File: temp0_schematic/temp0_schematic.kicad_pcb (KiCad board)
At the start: 2 copper layers, 64 x 94 mm, 16 parts, among them U1 Pro_Trinket_5V, U2 ESP-01, U3 oled_I2C_ssd1306, U4 hdc1080, U5 3.3V_REG

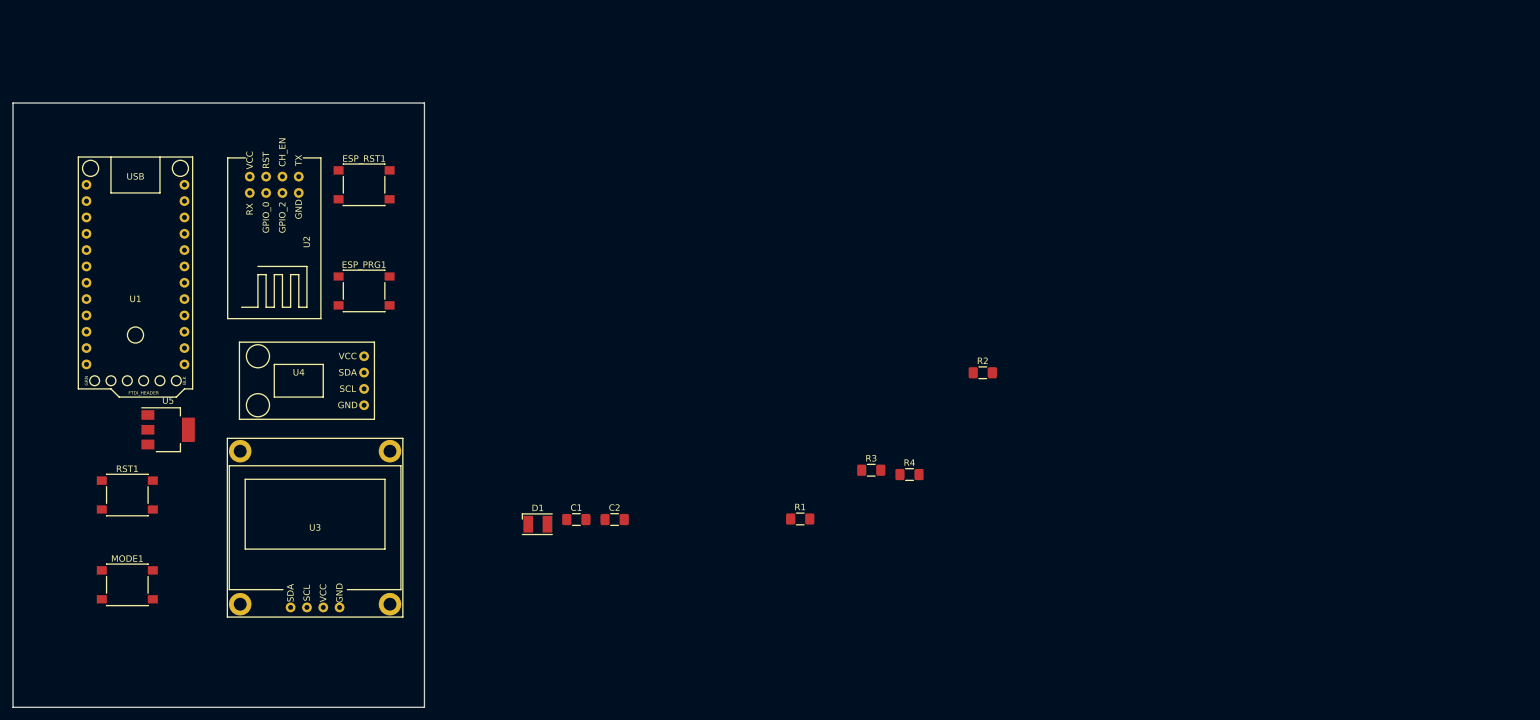
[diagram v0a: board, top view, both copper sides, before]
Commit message: Working on the schematic.  Added header for external button.
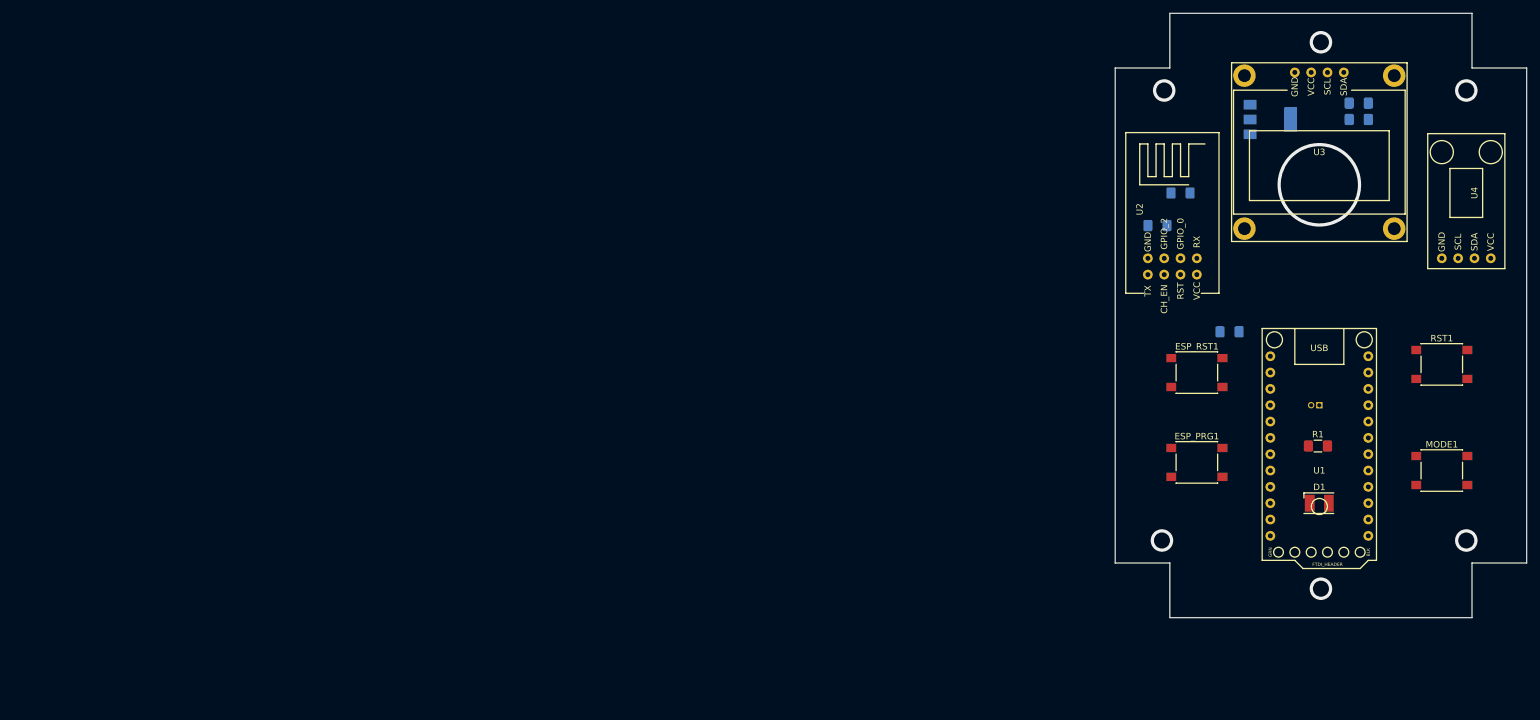
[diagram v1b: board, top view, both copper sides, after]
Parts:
- added J1: MODE1_EXT, Connector_PinHeader_1.27mm:PinHeader_1x02_P1.27mm_Horizontal, B.Cu at (233.7, 101.6)
- C1, C2, R2, R3, R4, U5: moved to B.Cu
- moved RST1 205.5 mm to (252.7, 95.2)
- moved MODE1 205.2 mm to (252.7, 111.8)
- moved U1 186.1 mm to (233.7, 108.0)
- moved U4 182.5 mm to (256.5, 69.8), turned to 90 degrees
- moved U5 178.1 mm to (226.1, 57.1)
- moved U3 166.8 mm to (233.7, 62.2), turned to 180 degrees
- moved U2 140.3 mm to (210.8, 80.0), turned to 270 degrees
- moved C1 137.9 mm to (239.8, 54.6)
- moved ESP_RST1 132.8 mm to (214.6, 96.5)
- moved ESP_PRG1 132.3 mm to (214.6, 110.5)
- moved C2 131.4 mm to (239.8, 57.1)
- moved D1 121.6 mm to (233.7, 116.8)
- moved R1 81.3 mm to (233.5, 108.0)
- moved R4 60.8 mm to (212.1, 68.6)
- moved R3 58.6 mm to (208.5, 73.7), turned to 180 degrees
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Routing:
- net (no net): vias 0 -> 7
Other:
- outline, holes or cut-outs redrawn

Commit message: Ran traces.
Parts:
- removed ESP_RST1: SW_Push, Button_Switch_SMD:SW_Push_1P1T_NO_6x6mm_H9.5mm
- added ESP_RST: SW_Push, Button_Switch_SMD:SW_Push_1P1T_NO_6x6mm_H9.5mm, F.Cu at (122.4, 105.4)
- J1: value MODE1_EXT -> MODE_EXT
- moved R2 96.8 mm to (123.2, 97.6), turned to 270 degrees
- moved U5 93.3 mm to (133.3, 67.3), turned to 270 degrees
- moved C2 93.0 mm to (147.5, 68.6)
- moved C1 92.8 mm to (147.5, 64.8)
- moved ESP_PRG 92.8 mm to (122.4, 120.7)
- moved U4 92.0 mm to (165.1, 80.0)
- moved R3 92.0 mm to (117.1, 83.8)
- moved U2 92.0 mm to (119.4, 90.2)
- moved U3 91.7 mm to (142.5, 72.0)
- moved D1 91.6 mm to (142.5, 125.7)
- moved U1 91.6 mm to (142.5, 116.8)
- moved R1 91.5 mm to (142.5, 118.1)
- moved J1 91.1 mm to (143.1, 111.8)
- moved RST 90.7 mm to (162.6, 105.4)
- moved MODE 90.6 mm to (162.6, 120.7)
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- renumbered ESP_PRG1 to ESP_PRG, MODE1 to MODE, RST1 to RST
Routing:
- net 3.3V: track 0.00 -> 100.4 mm, vias 0 -> 4
- net SCL: track 0.00 -> 94.1 mm
- net Net-(J1-Pad2): track 0.00 -> 90.0 mm
- net SDA: track 0.00 -> 87.8 mm
- net 5V: track 0.00 -> 70.4 mm
- net Net-(RST1-Pad2): track 0.00 -> 62.1 mm
- net Net-(ESP_PRG1-Pad2): track 0.00 -> 57.0 mm
- net U1_RX: track 0.00 -> 56.1 mm
- net U1_TX: track 0.00 -> 51.4 mm, vias 0 -> 1
- net Net-(ESP_RST1-Pad1): track 0.00 -> 22.3 mm, vias 0 -> 2
- net Net-(D1-Pad2): track 0.00 -> 15.3 mm, vias 0 -> 1
- net Net-(R3-Pad1): track 0.00 -> 8.98 mm
- net Net-(D1-Pad1): track 0.00 -> 7.63 mm
- added copper zone on B.Cu, net GND
- added copper zone on F.Cu, net GND
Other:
- net class Power added: clearance 0.2, trace_width 0.5, via_dia 1.6, via_drill 0.8

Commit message: Completed first attempt at pcb. Generated gerbers to order fab.
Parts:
- added G***: LOGO, temp0_parts:clewsy_logo_10mm, F.Cu at (149.9, 92.1)
- added U6: FTDI, Connector_PinHeader_2.54mm:PinHeader_1x06_P2.54mm_Horizontal, B.Cu at (128.3, 114.3)
- J1: footprint Connector_PinHeader_1.27mm:PinHeader_1x02_P1.27mm_Horizontal -> Connector_PinHeader_2.54mm:PinHeader_1x02_P2.54mm_Horizontal
- U3: value oled_I2C_ssd1306 -> SSD1306_128x64_OLED
- U4: value hdc1080 -> HDC1080
- moved J1 20.9 mm to (163.8, 114.3)
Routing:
- net 3.3V: track 100.4 -> 121.9 mm
- net U1_TX: track 51.4 -> 67.9 mm
- net Net-(J1-Pad2): track 90.0 -> 99.0 mm
- net U1_RX: track 56.1 -> 54.6 mm
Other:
- board text added: "clewsy 2020 clews.pro"

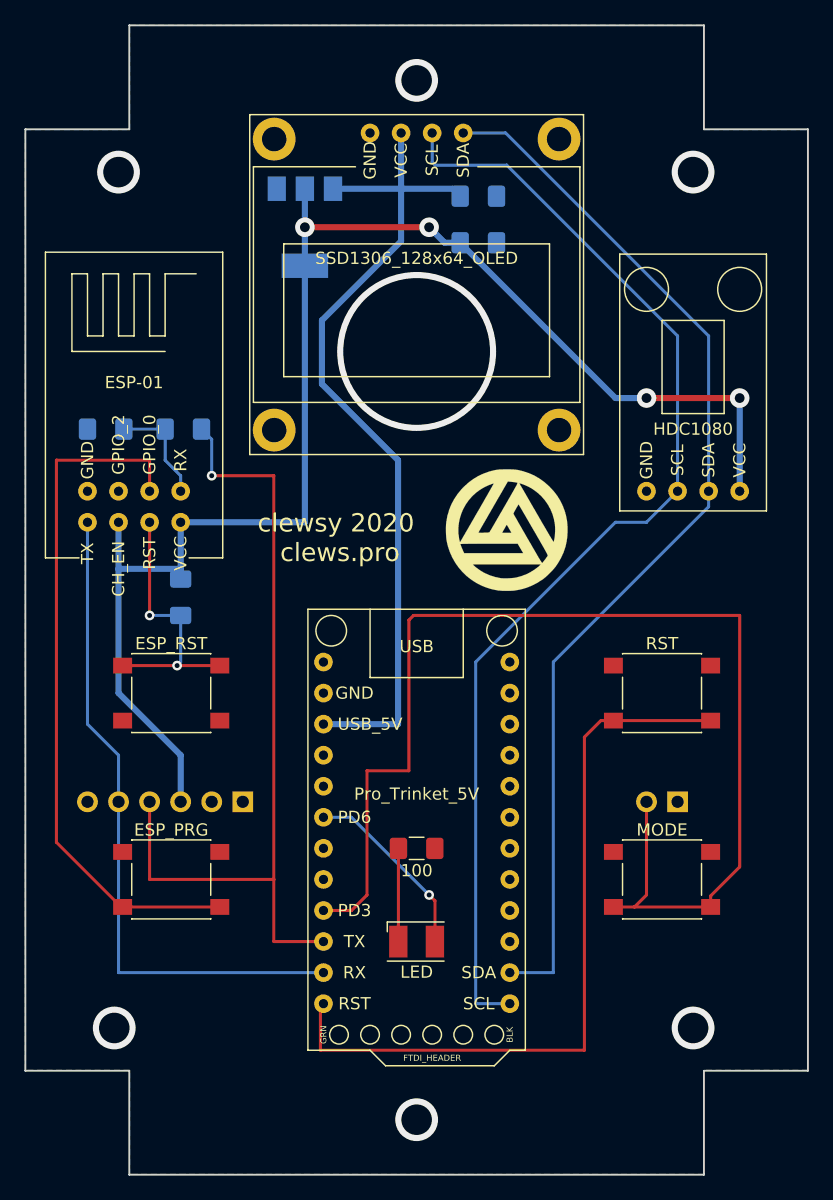
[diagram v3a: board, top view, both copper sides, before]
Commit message: PCB fixed - mount hole alignment, ftdi clearance, other.
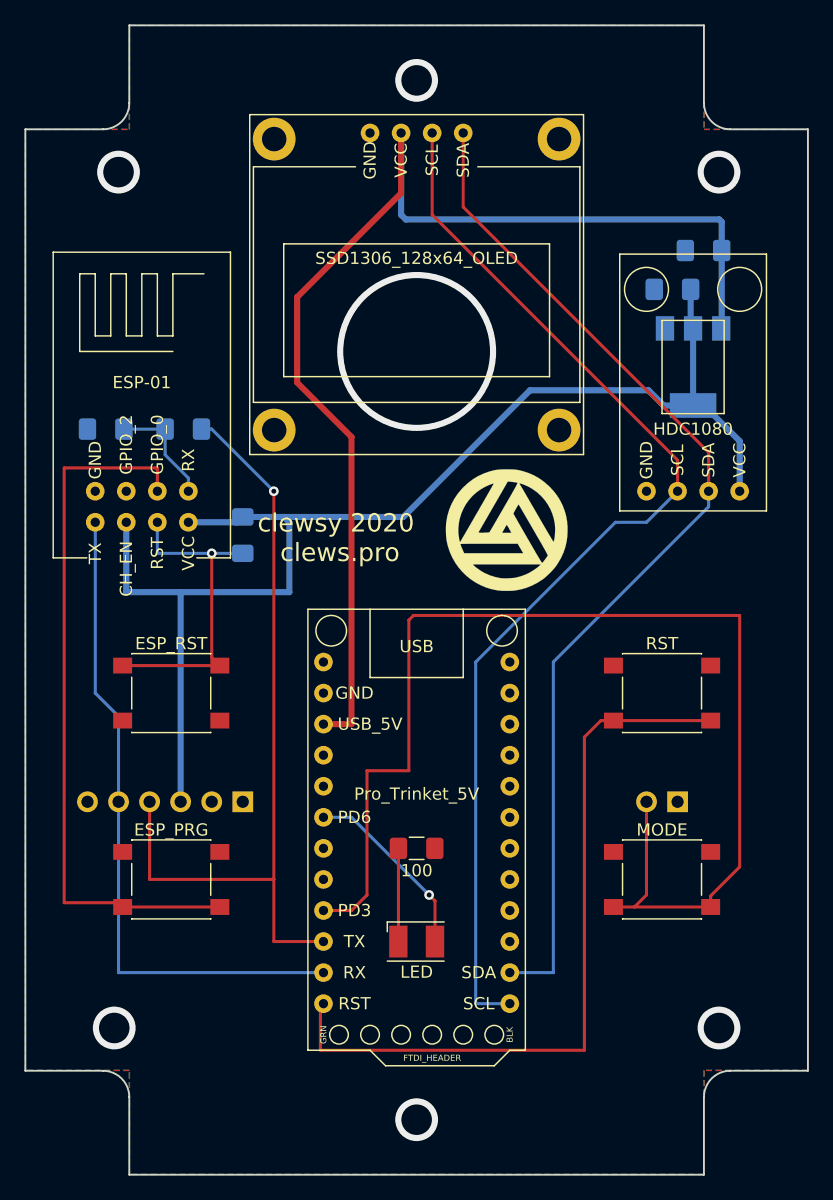
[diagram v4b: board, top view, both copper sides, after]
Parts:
- moved U5 33.7 mm to (165.1, 78.7)
- moved C1 18.9 mm to (166.0, 69.2), turned to 180 degrees
- moved C2 16.3 mm to (163.4, 72.4), turned to 180 degrees
- moved R2 7.18 mm to (128.3, 92.5)
- moved U2 0.64 mm to (120.0, 90.2)
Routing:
- net 5V: track 70.4 -> 97.9 mm
- net 3.3V: track 121.9 -> 107.5 mm, vias 4 -> 0
- net Net-(ESP_RST1-Pad1): track 22.3 -> 26.9 mm, vias 2 -> 1
- net SCL: track 94.1 -> 90.6 mm
- net U1_TX: track 67.9 -> 65.4 mm
- net SDA: track 87.8 -> 85.8 mm
- net Net-(ESP_PRG1-Pad2): track 57.0 -> 58.0 mm
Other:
- outline, holes or cut-outs redrawn
- board text added: "BLK"
- board text added: "GRN"

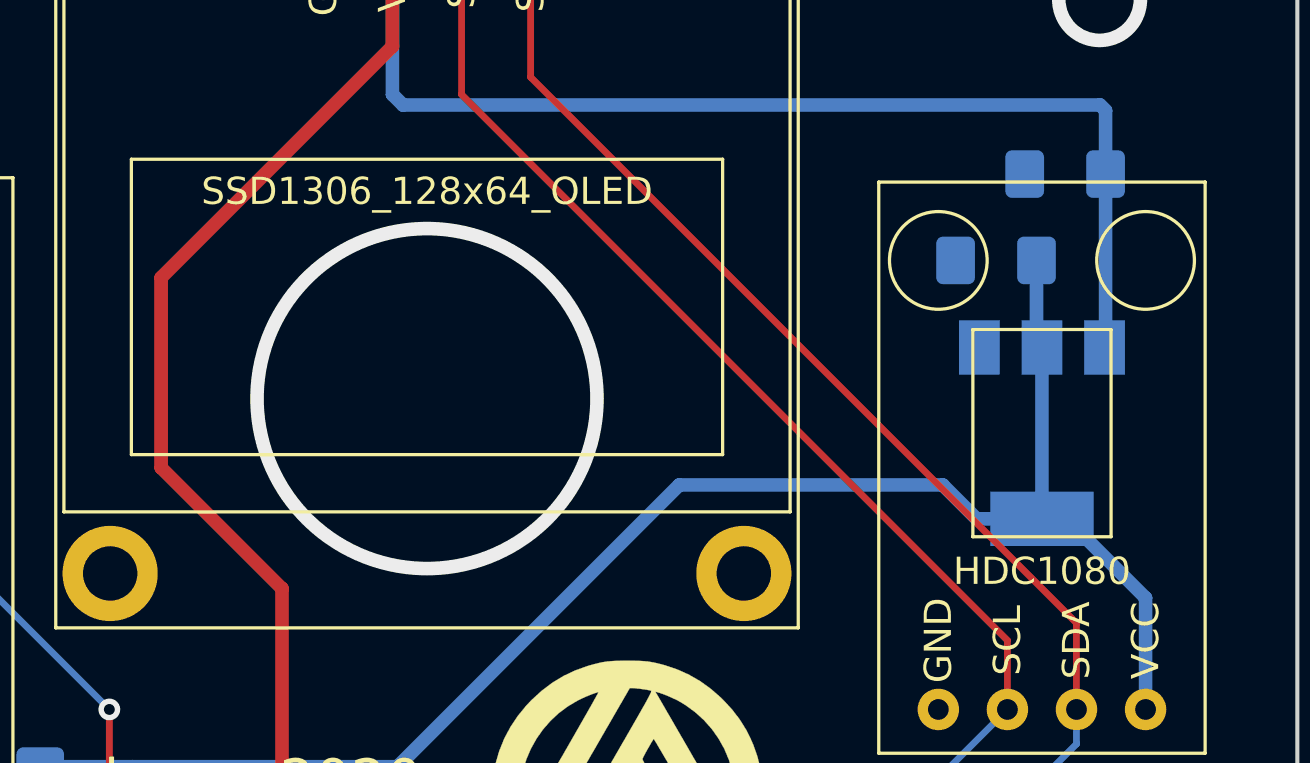
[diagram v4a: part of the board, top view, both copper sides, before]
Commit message: Tidied schematic and added pdf to repo.
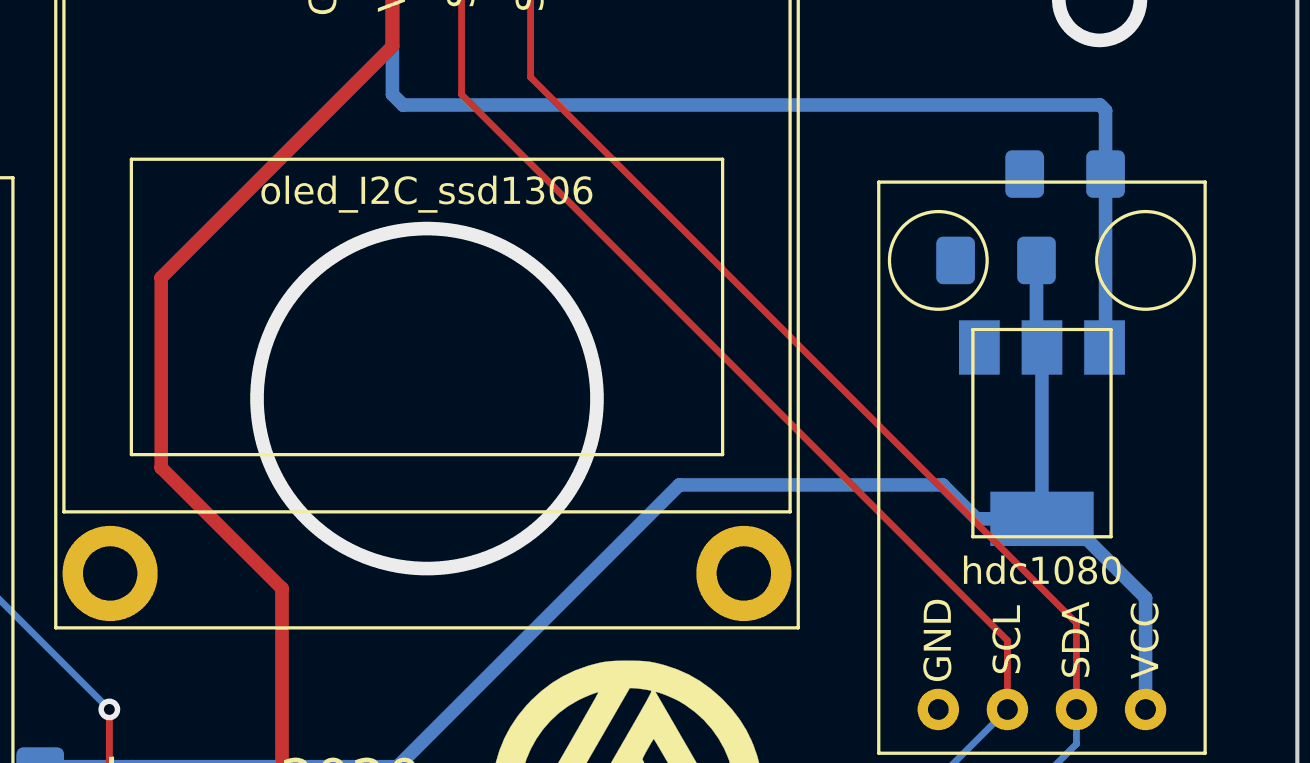
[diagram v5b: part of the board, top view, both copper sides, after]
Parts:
- U3: value SSD1306_128x64_OLED -> oled_I2C_ssd1306
- U4: value HDC1080 -> hdc1080
- U6: value FTDI -> ftdi_header
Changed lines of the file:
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@@
       (effects (font (size 1 1) (thickness 0.15)))
     )
-    (fp_text value SSD1306_128x64_OLED (at 0 2.15) (layer F.SilkS)
+    (fp_text value oled_I2C_ssd1306 (at 0 2.15) (layer F.SilkS)
       (effects (font (size 1 1) (thickness 0.15)))
     )
@@
       (effects (font (size 1 1) (thickness 0.15)) (justify mirror))
     )
-    (fp_text value FTDI (at -2.54 -6.35) (layer B.SilkS)
+    (fp_text value ftdi_header (at -2.54 -6.35) (layer B.SilkS)
       (effects (font (size 1 1) (thickness 0.15)) (justify mirror))
     )
@@
       (effects (font (size 1 1) (thickness 0.15)))
     )
-    (fp_text value HDC1080 (at -3.81 0 180) (layer F.SilkS)
-      (effects (font (size 1 1) (thickness 0.15)))
-    )
+    (fp_text value hdc1080 (at -3.81 0 180) (layer F.SilkS)
+      (effects (font (size 1 1) (thickness 0.15)))
+    )

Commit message: Schematic and PCB revision 2.
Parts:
- removed ESP_PRG, ESP_RST: SW_Push, Button_Switch_SMD:SW_Push_1P1T_NO_6x6mm_H9.5mm
- removed the G*** at (149.9, 92.1)
- removed R2: 10k, Resistor_SMD:R_1206_3216Metric_Pad1.42x1.75mm_HandSolder
- removed U6: ftdi_header, Connector_PinHeader_2.54mm:PinHeader_1x06_P2.54mm_Horizontal
- added G***: LOGO, temp0_parts:oshw_logo_10mm, F.Cu at (165.4, 73.9)
- added G***: LOGO, temp0_parts:oshw_logo_10mm, B.Cu at (160.3, 72.6)
- added G***: LOGO, temp0_parts:clewsy_logo_10mm, B.Cu at (142.7, 93.0)
- added G***: LOGO, temp0_parts:clewsy_logo_10mm, F.Cu at (119.9, 72.5)
- moved C1 44.7 mm to (121.4, 65.3)
- moved U5 44.5 mm to (120.7, 75.9)
- moved C2 44.4 mm to (119.2, 68.8)
- moved RST 41.9 mm to (122.5, 93.0)
- moved U4 35.9 mm to (162.9, 115.8)
- moved R3 34.0 mm to (122.6, 117.3)
- moved R4 33.9 mm to (128.6, 117.3)
- moved U2 33.6 mm to (122.0, 123.7)
- moved MODE 27.7 mm to (162.5, 93.0)
- moved J1 14.3 mm to (163.8, 100.0)
- moved R1 3.89 mm to (142.5, 122.0), turned to 180 degrees
- moved D1 1.77 mm to (142.5, 127.5), turned to 180 degrees
- moved U1 1.66 mm to (142.5, 118.5)
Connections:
- U2 pad 6: Net-(ESP_RST1-Pad1) -> 3.3V
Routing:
- net Net-(U2-Pad5): track 58.0 -> 0.00 mm
- net U1_TX: track 65.4 -> 12.0 mm
- net Net-(J1-Pad2): track 99.0 -> 57.8 mm
- net U1_RX: track 54.4 -> 18.7 mm
- net Net-(ESP_RST1-Pad1): track 26.9 -> 0.00 mm, vias 1 -> 0
- net 5V: track 97.9 -> 75.0 mm
- net 3.3V: track 107.5 -> 126.7 mm
- net Net-(RST1-Pad2): track 62.1 -> 50.0 mm, vias 0 -> 1
- net SDA: track 85.8 -> 97.6 mm
- net SCL: track 90.6 -> 88.0 mm
- net Net-(D1-Pad1): track 7.63 -> 5.51 mm
- net Net-(D1-Pad2): track 15.3 -> 14.0 mm, vias 1 -> 0
- net Net-(R3-Pad1): track 9.24 -> 8.18 mm
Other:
- board text added: "2"
- board text added: "clews.pro"
- board text added: "temp0 PCB layout"
- board text removed: "BLK"
- board text removed: "GRN"
- board text removed: "clewsy 2020 clews.pro"
